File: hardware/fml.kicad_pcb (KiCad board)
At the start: 2 copper layers, 1 part, among them U1 Teensy3.6

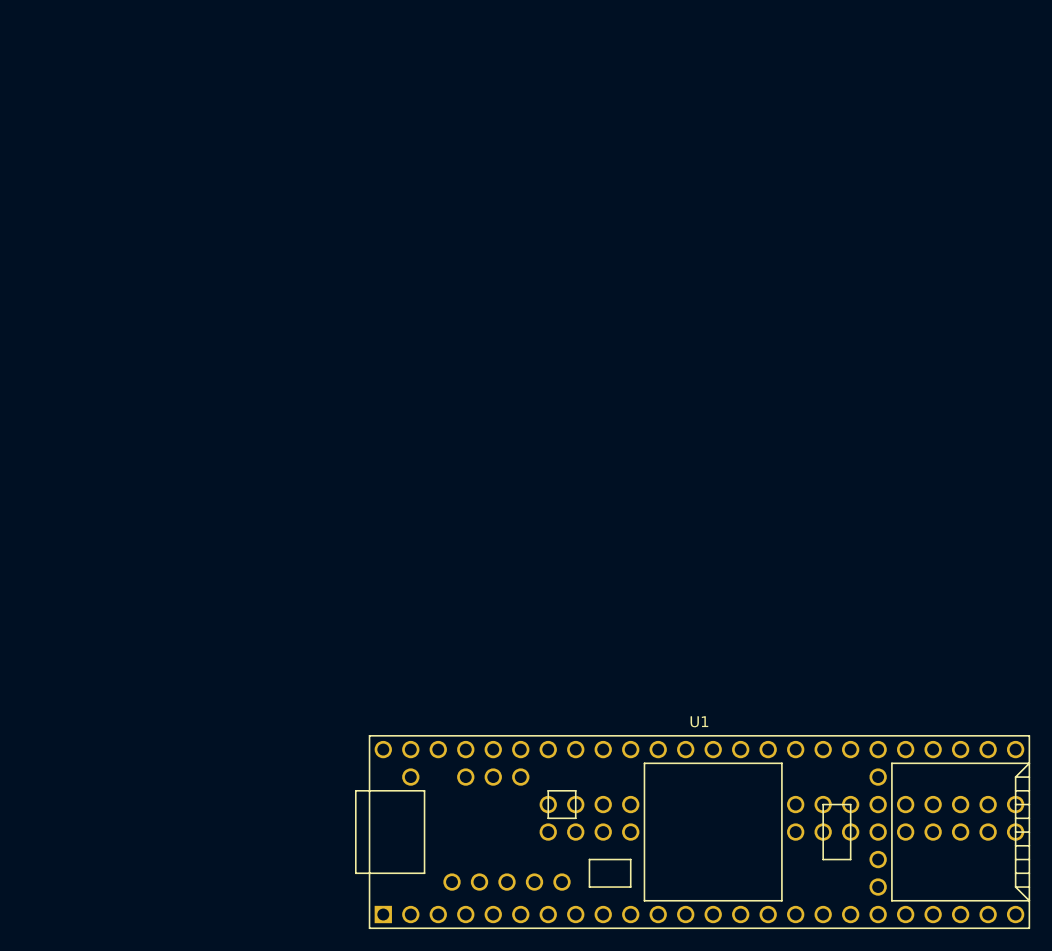
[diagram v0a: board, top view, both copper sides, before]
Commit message: hooked up midi in and out
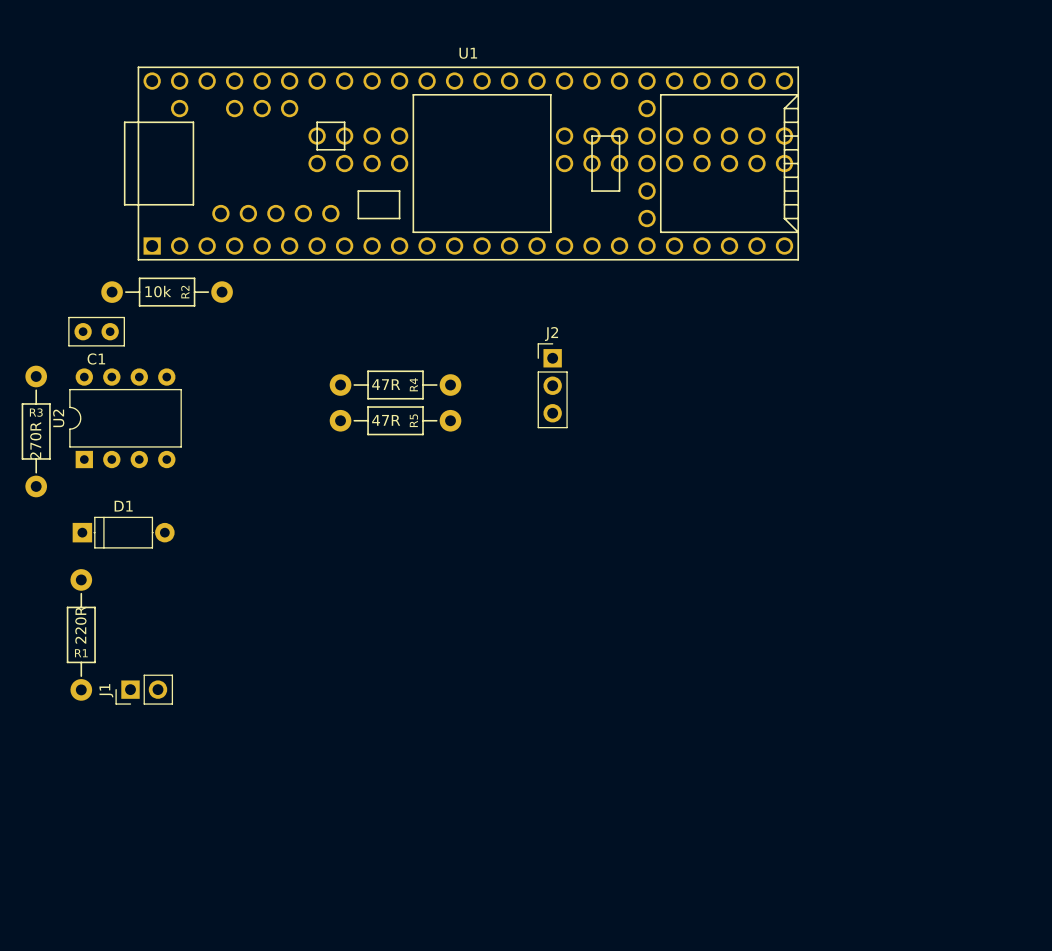
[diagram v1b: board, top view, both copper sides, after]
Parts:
- added C1: 0.1u, Capacitors_ThroughHole:C_Disc_D5.0mm_W2.5mm_P2.50mm, F.Cu at (94.1, 58.8)
- added D1: 1n914, Diodes_ThroughHole:D_A-405_P7.62mm_Horizontal, F.Cu at (91.5, 77.3)
- added J1: midi_in, Pin_Headers:Pin_Header_Straight_1x02_Pitch2.54mm, F.Cu at (95.9, 91.8)
- added J2: midi_out, Pin_Headers:Pin_Header_Straight_1x03_Pitch2.54mm, F.Cu at (134.9, 61.2)
- added R1: 220R, xnorman:Resistor_Horizontal_RM10mm-xnorman, F.Cu at (91.4, 81.7)
- added R2: 10k, xnorman:Resistor_Horizontal_RM10mm-xnorman, F.Cu at (94.2, 55.1)
- added R3: 270R, xnorman:Resistor_Horizontal_RM10mm-xnorman, F.Cu at (87.2, 73.1)
- added R4: 47R, xnorman:Resistor_Horizontal_RM10mm-xnorman, F.Cu at (115.3, 63.7)
- added R5: 47R, xnorman:Resistor_Horizontal_RM10mm-xnorman, F.Cu at (115.3, 67.0)
- added U2: 6N138, Housings_DIP:DIP-8_W7.62mm, F.Cu at (91.7, 70.6)
- moved U1 65.4 mm to (127.1, 43.2)
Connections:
- U1 pad 1: (no net) -> GND
- U1 pad 2: (no net) -> Net-(R3-Pad2)
- U1 pad 3: (no net) -> Net-(R5-Pad1)
- U1 pad 58: (no net) -> 5v
- U1 pad 61: (no net) -> GND
- U1 pad 62: (no net) -> GND
- U1 pad 74: (no net) -> GND
- U1 pad 75: (no net) -> 3.3v

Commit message: pcb updates
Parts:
- added J3: pins, Pin_Headers:Pin_Header_Straight_1x24_Pitch2.54mm, F.Cu at (98.0, 54.4)
- added J4: pins, Pin_Headers:Pin_Header_Straight_1x24_Pitch2.54mm, F.Cu at (98.0, 31.5)
- moved R2 4.67 mm to (97.2, 58.7)
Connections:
- U1 pad 10: (no net) -> Net-(J3-Pad10)
- U1 pad 11: (no net) -> Net-(J3-Pad11)
- U1 pad 12: (no net) -> Net-(J3-Pad12)
- U1 pad 13: (no net) -> Net-(J3-Pad13)
- U1 pad 14: (no net) -> Net-(J3-Pad14)
- U1 pad 15: (no net) -> 3.3v
- U1 pad 16: (no net) -> Net-(J3-Pad16)
- U1 pad 17: (no net) -> Net-(J3-Pad17)
- U1 pad 18: (no net) -> Net-(J3-Pad18)
- U1 pad 19: (no net) -> Net-(J3-Pad19)
- U1 pad 20: (no net) -> Net-(J3-Pad20)
- U1 pad 21: (no net) -> Net-(J3-Pad21)
- U1 pad 22: (no net) -> Net-(J3-Pad22)
- U1 pad 23: (no net) -> Net-(J3-Pad23)
- U1 pad 24: (no net) -> Net-(J3-Pad24)
- U1 pad 26: (no net) -> 3.3v
- U1 pad 27: (no net) -> GND
- U1 pad 30: (no net) -> Net-(J4-Pad24)
- U1 pad 31: (no net) -> Net-(J4-Pad23)
- U1 pad 32: (no net) -> Net-(J4-Pad22)
- U1 pad 33: (no net) -> Net-(J4-Pad21)
- U1 pad 34: (no net) -> Net-(J4-Pad20)
- U1 pad 35: (no net) -> Net-(J4-Pad19)
- U1 pad 36: (no net) -> Net-(J4-Pad18)
- U1 pad 37: (no net) -> Net-(J4-Pad17)
- U1 pad 38: (no net) -> Net-(J4-Pad16)
- U1 pad 39: (no net) -> GND
- U1 pad 4: (no net) -> Net-(J3-Pad4)
- U1 pad 40: (no net) -> Net-(J4-Pad14)
- U1 pad 41: (no net) -> Net-(J4-Pad13)
- U1 pad 42: (no net) -> Net-(J4-Pad12)
- U1 pad 43: (no net) -> Net-(J4-Pad11)
- U1 pad 44: (no net) -> Net-(J4-Pad10)
- U1 pad 45: (no net) -> Net-(J4-Pad9)
- U1 pad 46: (no net) -> Net-(J4-Pad8)
- U1 pad 47: (no net) -> Net-(J4-Pad7)
- U1 pad 48: (no net) -> Net-(J4-Pad6)
- U1 pad 49: (no net) -> Net-(J4-Pad5)
- U1 pad 5: (no net) -> Net-(J3-Pad5)
- U1 pad 50: (no net) -> Net-(J4-Pad4)
- U1 pad 51: (no net) -> Net-(J4-Pad3)
- U1 pad 52: (no net) -> Net-(J4-Pad2)
- U1 pad 53: (no net) -> Net-(J4-Pad1)
- U1 pad 6: (no net) -> Net-(J3-Pad6)
- U1 pad 7: (no net) -> Net-(J3-Pad7)
- U1 pad 74: GND -> (no net)
- U1 pad 75: 3.3v -> (no net)
- U1 pad 8: (no net) -> Net-(J3-Pad8)
- U1 pad 9: (no net) -> Net-(J3-Pad9)

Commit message: moved some pcb stuff around
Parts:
- moved J1 41.3 mm to (130.9, 69.8)
- moved R1 31.2 mm to (121.6, 73.9), turned to 90 degrees
- moved R5 22.0 mm to (137.4, 66.0)
- moved R4 22.0 mm to (137.4, 62.7)
- moved D1 19.2 mm to (110.4, 73.8)
- moved C1 17.9 mm to (112.0, 58.3)
- moved R2 17.9 mm to (115.1, 58.3)
- moved R3 17.9 mm to (105.1, 72.6)
- moved U2 17.9 mm to (109.6, 70.2)
- moved J2 9.63 mm to (139.7, 69.6), turned to 90 degrees
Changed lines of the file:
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@@
     (links 72)
     (no_connects 72)
-    (area 0 0 0 0)
+    (area 85.498599 29.496399 159.7928 94.713066)
     (thickness 1.6)
     (drawings 0)
@@
   )
   (module Capacitors_ThroughHole:C_Disc_D5.0mm_W2.5mm_P2.50mm (layer F.Cu)
-    (at 94.0562 58.7756 180)
+    (at 111.9632 58.3438 180)
     (descr "C, Disc series, Radial, pin pitch=2.50mm, , diameter*width=5*2.5mm^2, Capacitor, http://cdn-reichelt.de/documents/datenblatt/B300/DS_KERKO_TC.pdf")
     (tags "C Disc series Radial pin pitch 2.50mm  diameter 5mm width 2.5mm Capacitor")
@@
   )
   (module Diodes_ThroughHole:D_A-405_P7.62mm_Horizontal (layer F.Cu)
-    (at 91.4908 77.343)
+    (at 110.363 73.8124)
     (descr "D, A-405 series, Axial, Horizontal, pin pitch=7.62mm, , length*diameter=5.2*2.7mm^2, , http://www.diodes.com/_files/packages/A-405.pdf")
     (tags "D A-405 series Axial Horizontal pin pitch 7.62mm  length 5.2mm diameter 2.7mm")
@@
   )
   (module Pin_Headers:Pin_Header_Straight_1x02_Pitch2.54mm (layer F.Cu)
-    (at 95.9358 91.8464 90)
+    (at 130.9116 69.8246 90)
     (descr "Through hole straight pin header, 1x02, 2.54mm pitch, single row")
     (tags "Through hole pin header THT 1x02 2.54mm single row")
@@
   )
   (module Pin_Headers:Pin_Header_Straight_1x03_Pitch2.54mm (layer F.Cu)
-    (at 134.939666 61.2306)
+    (at 139.6746 69.6214 90)
     (descr "Through hole straight pin header, 1x03, 2.54mm pitch, single row")
     (tags "Through hole pin header THT 1x03 2.54mm single row")
-    (fp_text reference J2 (at 0 -2.33) (layer F.SilkS)
-      (effects (font (size 1 1) (thickness 0.15)))
-    )
-    (fp_text value midi_out (at 0 7.41) (layer F.Fab)
+    (fp_text reference J2 (at 0 -2.33 90) (layer F.SilkS)
+      (effects (font (size 1 1) (thickness 0.15)))
+    )
+    (fp_text value midi_out (at 0 7.41 90) (layer F.Fab)
       (effects (font (size 1 1) (thickness 0.15)))
     )
@@
     (fp_line (start 1.8 6.85) (end 1.8 -1.8) (layer F.CrtYd) (width 0.05))
     (fp_line (start 1.8 -1.8) (end -1.8 -1.8) (layer F.CrtYd) (width 0.05))
-    (fp_text user %R (at 0 2.54 90) (layer F.Fab)
-      (effects (font (size 1 1) (thickness 0.15)))
-    )
-    (pad 1 thru_hole rect (at 0 0) (size 1.7 1.7) (drill 1) (layers *.Cu *.Mask)
+    (fp_text user %R (at 0 2.54 180) (layer F.Fab)
+      (effects (font (size 1 1) (thickness 0.15)))
+    )
+    (pad 1 thru_hole rect (at 0 0 90) (size 1.7 1.7) (drill 1) (layers *.Cu *.Mask)
       (net 1 GND))
-    (pad 2 thru_hole oval (at 0 2.54) (size 1.7 1.7) (drill 1) (layers *.Cu *.Mask)
+    (pad 2 thru_hole oval (at 0 2.54 90) (size 1.7 1.7) (drill 1) (layers *.Cu *.Mask)
       (net 6 "Net-(J2-Pad2)"))
-    (pad 3 thru_hole oval (at 0 5.08) (size 1.7 1.7) (drill 1) (layers *.Cu *.Mask)
+    (pad 3 thru_hole oval (at 0 5.08 90) (size 1.7 1.7) (drill 1) (layers *.Cu *.Mask)
       (net 7 "Net-(J2-Pad3)"))
     (model ${KISYS3DMOD}/Pin_Headers.3dshapes/Pin_Header_Straight_1x03_Pitch2.54mm.wrl
@@
   )
   (module xnorman:Resistor_Horizontal_RM10mm-xnorman (layer F.Cu)
-    (at 91.3892 81.7118 270)
+    (at 121.5898 73.9394 90)
     (descr "Resistor, Axial,  RM 10mm, 1/3W")
     (tags "Resistor Axial RM 10mm 1/3W")
-    (fp_text reference R1 (at 6.8 0 360) (layer F.SilkS)
+    (fp_text reference R1 (at 6.8 0 180) (layer F.SilkS)
       (effects (font (size 0.75 0.75) (thickness 0.15)))
     )
-    (fp_text value 220R (at 4.2 0 270) (layer F.SilkS)
+    (fp_text value 220R (at 4.2 0 90) (layer F.SilkS)
       (effects (font (size 1 1) (thickness 0.15)))
     )
@@
     (fp_line (start 2.54 0) (end 1.27 0) (layer F.SilkS) (width 0.15))
     (fp_line (start 7.62 0) (end 8.89 0) (layer F.SilkS) (width 0.15))
-    (pad 1 thru_hole circle (at 0 0 270) (size 1.99898 1.99898) (drill 1.00076) (layers *.Cu *.SilkS *.Mask)
+    (pad 1 thru_hole circle (at 0 0 90) (size 1.99898 1.99898) (drill 1.00076) (layers *.Cu *.SilkS *.Mask)
       (net 3 "Net-(D1-Pad1)"))
-    (pad 2 thru_hole circle (at 10.16 0 270) (size 1.99898 1.99898) (drill 1.00076) (layers *.Cu *.SilkS *.Mask)
+    (pad 2 thru_hole circle (at 10.16 0 90) (size 1.99898 1.99898) (drill 1.00076) (layers *.Cu *.SilkS *.Mask)
       (net 5 "Net-(J1-Pad1)"))
     (model Resistors_ThroughHole.3dshapes/Resistor_Horizontal_RM10mm.wrl
@@
   )
   (module xnorman:Resistor_Horizontal_RM10mm-xnorman (layer F.Cu)
-    (at 97.2058 58.7248)
+    (at 115.1128 58.293)
     (descr "Resistor, Axial,  RM 10mm, 1/3W")
     (tags "Resistor Axial RM 10mm 1/3W")
@@
   )
   (module xnorman:Resistor_Horizontal_RM10mm-xnorman (layer F.Cu)
-    (at 87.2236 73.0758 90)
+    (at 105.1306 72.644 90)
     (descr "Resistor, Axial,  RM 10mm, 1/3W")
     (tags "Resistor Axial RM 10mm 1/3W")
@@
   )
   (module xnorman:Resistor_Horizontal_RM10mm-xnorman (layer F.Cu)
-    (at 115.3414 63.7032)
+    (at 137.3632 62.6872)
     (descr "Resistor, Axial,  RM 10mm, 1/3W")
     (tags "Resistor Axial RM 10mm 1/3W")
@@
   )
   (module xnorman:Resistor_Horizontal_RM10mm-xnorman (layer F.Cu)
-    (at 115.3414 67.0052)
+    (at 137.3632 65.9638)
     (descr "Resistor, Axial,  RM 10mm, 1/3W")
     (tags "Resistor Axial RM 10mm 1/3W")
@@
   )
   (module Housings_DIP:DIP-8_W7.62mm (layer F.Cu)
-    (at 91.6686 70.5866 90)
+    (at 109.5756 70.1548 90)
     (descr "8-lead though-hole mounted DIP package, row spacing 7.62 mm (300 mils)")
     (tags "THT DIP DIL PDIP 2.54mm 7.62mm 300mil")
